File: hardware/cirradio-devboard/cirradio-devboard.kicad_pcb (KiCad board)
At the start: 10 copper layers, 0 parts

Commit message: configure 10-layer stackup and design rules
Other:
- board outline added: 160 x 100 mm
- net class DDR3 added: clearance 0.1, trace_width 0.1, via_dia 0.45, via_drill 0.2
- net class DDR3_DiffPair added: clearance 0.1, trace_width 0.1, via_dia 0.45, via_drill 0.2
- net class Default added: clearance 0.1, trace_width 0.15, via_dia 0.55, via_drill 0.3
- net class LVDS added: clearance 0.12, trace_width 0.12, via_dia 0.45, via_drill 0.2
- net class Power added: clearance 0.2, trace_width 0.4, via_dia 0.7, via_drill 0.4
- net class Power_Wide added: clearance 0.2, trace_width 0.8, via_dia 0.7, via_drill 0.4
- net class RF_50ohm added: clearance 0.2, trace_width 0.28, via_dia 0.55, via_drill 0.3
- board text added: "IMPEDANCE TARGETS: 50u03A9 microstrip (F.Cu): 0.28mm w, ref GND1 100u03A9 diff stripline (In2.Cu): 0.12mm w, 0.20mm gap 50u03A9 stripline (In2/In4.Cu): 0.18mm w"
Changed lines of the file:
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@@
     (pad_to_mask_clearance 0)
     (allow_soldermask_bridges_in_footprints no)
+    (stackup
+      (layer "F.Cu" (type "copper") (thickness 0.035))
+      (layer "dielectric 1" (type "prepreg") (thickness 0.1) (epsilon_r 4.2))
+      (layer "In1.Cu" (type "copper") (thickness 0.035))
+      (layer "dielectric 2" (type "core") (thickness 0.2) (epsilon_r 4.5))
+      (layer "In2.Cu" (type "copper") (thickness 0.035))
+      (layer "dielectric 3" (type "prepreg") (thickness 0.1) (epsilon_r 4.2))
+      (layer "In3.Cu" (type "copper") (thickness 0.035))
+      (layer "dielectric 4" (type "core") (thickness 0.2) (epsilon_r 4.5))
+      (layer "In4.Cu" (type "copper") (thickness 0.035))
+      (layer "dielectric 5" (type "prepreg") (thickness 0.1) (epsilon_r 4.2))
+      (layer "In5.Cu" (type "copper") (thickness 0.035))
+      (layer "dielectric 6" (type "core") (thickness 0.2) (epsilon_r 4.5))
+      (layer "In6.Cu" (type "copper") (thickness 0.035))
+      (layer "dielectric 7" (type "prepreg") (thickness 0.1) (epsilon_r 4.2))
+      (layer "In7.Cu" (type "copper") (thickness 0.035))
+      (layer "dielectric 8" (type "core") (thickness 0.2) (epsilon_r 4.5))
+      (layer "In8.Cu" (type "copper") (thickness 0.035))
+      (layer "dielectric 9" (type "prepreg") (thickness 0.1) (epsilon_r 4.2))
+      (layer "B.Cu" (type "copper") (thickness 0.035))
+      (copper_finish "ENIG")
+      (dielectric_constraints yes)
+    )
     (pcbplotparams
       (layerselection 0x00010fc_ffffffff)
@@
   (net 0 "")
   (net 1 "GND")
+  (net_class "Default" ""
+    (clearance 0.1)
+    (trace_width 0.15)
+    (via_dia 0.55)
+    (via_drill 0.3)
+    (uvia_dia 0.3)
+    (uvia_drill 0.1)
+  )
+  (net_class "Power" ""
+    (clearance 0.2)
+    (trace_width 0.4)
+    (via_dia 0.7)
+    (via_drill 0.4)
+    (uvia_dia 0.3)
+    (uvia_drill 0.1)
+  )
+  (net_class "Power_Wide" ""
+    (clearance 0.2)
+    (trace_width 0.8)
+    (via_dia 0.7)
+    (via_drill 0.4)
+    (uvia_dia 0.3)
+    (uvia_drill 0.1)
+  )
+  (net_class "RF_50ohm" ""
+    (clearance 0.2)
+    (trace_width 0.28)
+    (via_dia 0.55)
+    (via_drill 0.3)
+    (uvia_dia 0.3)
+    (uvia_drill 0.1)
+  )
+  (net_class "LVDS" ""
+    (clearance 0.12)
+    (trace_width 0.12)
+    (via_dia 0.45)
+    (via_drill 0.2)
+    (uvia_dia 0.3)
+    (uvia_drill 0.1)
+    (diff_pair_width 0.12)
+    (diff_pair_gap 0.2)
+  )
+  (net_class "DDR3" ""
+    (clearance 0.1)
+    (trace_width 0.1)
+    (via_dia 0.45)
+    (via_drill 0.2)
+    (uvia_dia 0.3)
+    (uvia_drill 0.1)
+  )
+  (net_class "DDR3_DiffPair" ""
+    (clearance 0.1)
+    (trace_width 0.1)
+    (via_dia 0.45)
+    (via_drill 0.2)
+    (uvia_dia 0.3)
+    (uvia_drill 0.1)
+    (diff_pair_width 0.1)
+    (diff_pair_gap 0.15)
+  )
+  (gr_rect (start 0 0) (end 160 100) (stroke (width 0.1) (type solid)) (fill none) (layer "Edge.Cuts"))
+  (gr_text "IMPEDANCE TARGETS:\n50\u03A9 microstrip (F.Cu): 0.28mm w, ref GND1\n100\u03A9 diff stripline (In2.Cu): 0.12mm w, 0.20mm gap\n50\u03A9 stripline (In2/In4.Cu): 0.18mm w"
+    (at 80 -5) (layer "Cmts.User")
+    (effects (font (size 1.5 1.5) (thickness 0.15)))
+  )
 )

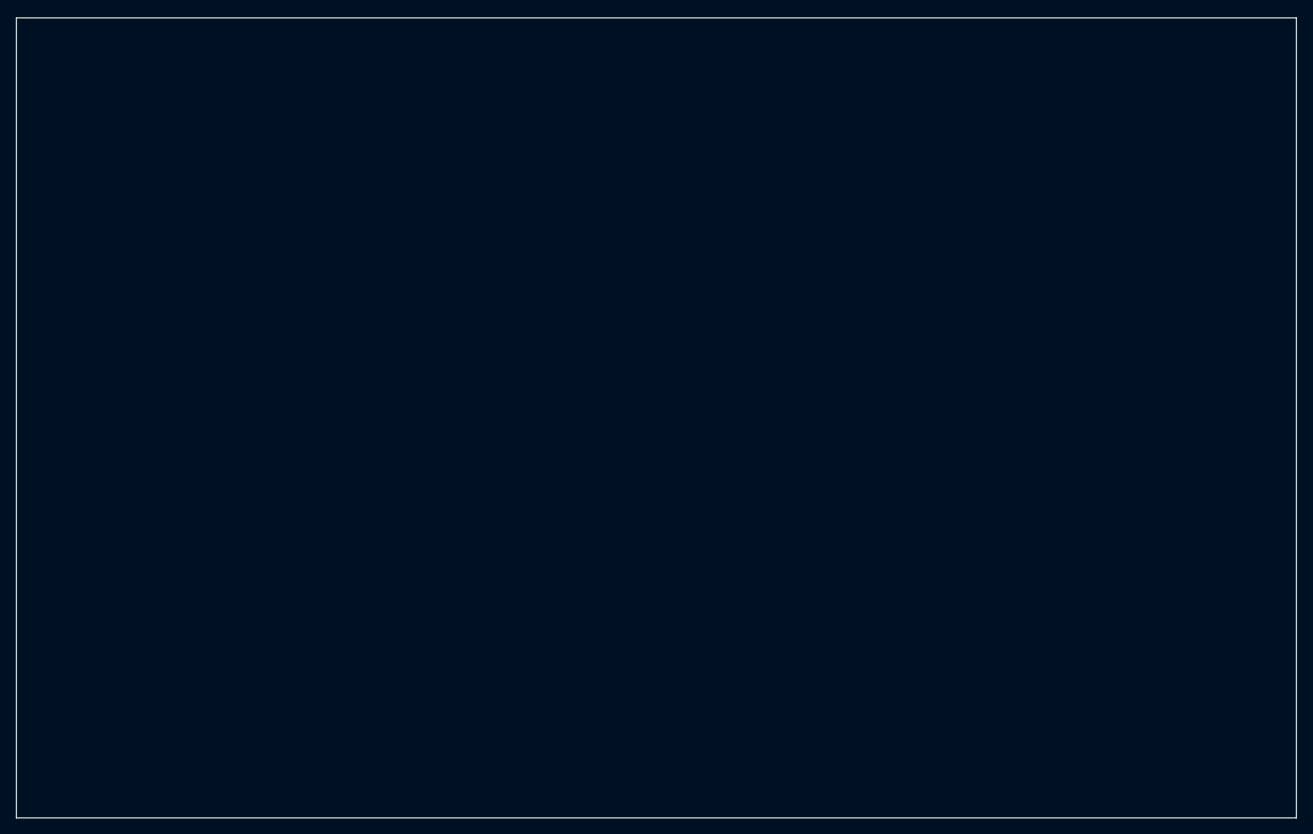
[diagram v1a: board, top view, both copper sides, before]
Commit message: add PCB netlist import with board setup
312 components, 433 nets parsed from schematics.
10-layer stackup, net classes (DDR3, LVDS, RF, Power),
160x100mm board outline, 4x M3 mounting holes.
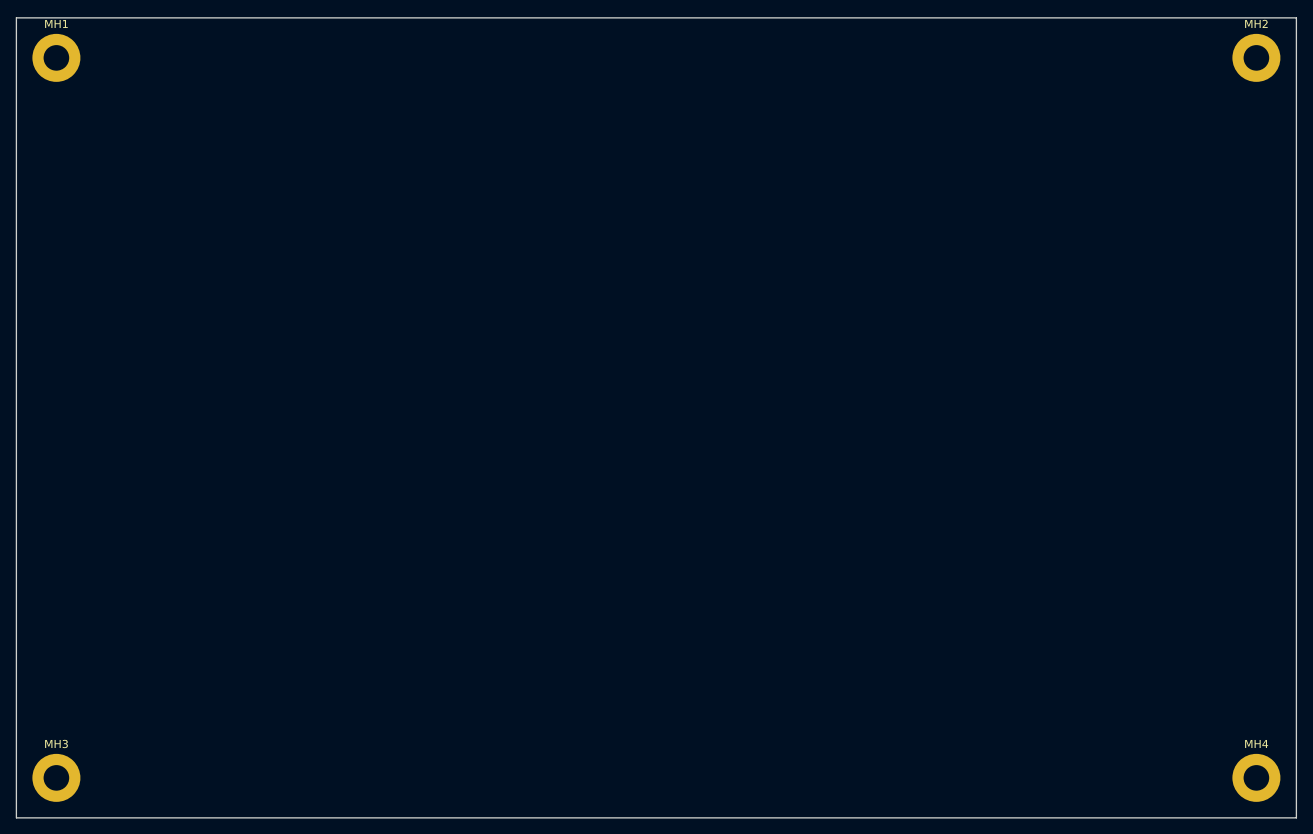
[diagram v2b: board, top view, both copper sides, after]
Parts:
- added MH1: MountingHole_3.2mm_M3_Pad, MountingHole:MountingHole_3.2mm_M3_Pad, F.Cu at (5.00, 5.00)
- added MH2: MountingHole_3.2mm_M3_Pad, MountingHole:MountingHole_3.2mm_M3_Pad, F.Cu at (155.0, 5.00)
- added MH3: MountingHole_3.2mm_M3_Pad, MountingHole:MountingHole_3.2mm_M3_Pad, F.Cu at (5.00, 95.0)
- added MH4: MountingHole_3.2mm_M3_Pad, MountingHole:MountingHole_3.2mm_M3_Pad, F.Cu at (155.0, 95.0)
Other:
- board text added: "NETLIST IMPORT SUMMARY: Total components: 312 Total nets: 433 ICs: 16, Caps: 181, Res: 72, Ind: 13, Diodes: 4, LEDs: 4 Connectors: 7, Crystals: 3 Note: Run Update PCB from Schematic to import component footprints"

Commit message: add component placement generator
312 components placed across 7 zones: RF front-end,
AD9361, Zynq center, DDR3L, power supply, GPS,
connectors. Decoupling caps on B.Cu under BGAs.
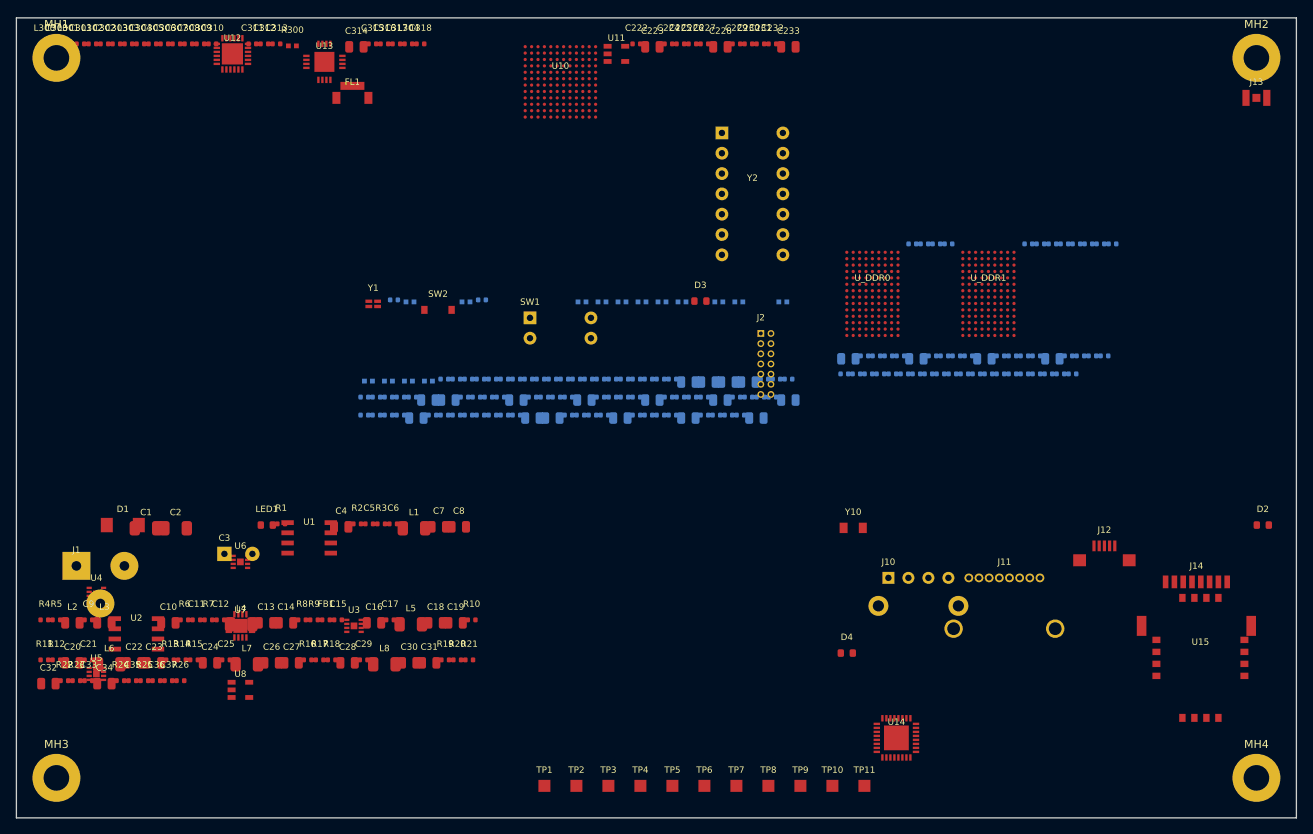
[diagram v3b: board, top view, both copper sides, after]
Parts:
- added C1: 100uF, Capacitor_SMD:C_1206_3216Metric, F.Cu at (16.2, 63.8)
- added C10: 10uF, Capacitor_SMD:C_0805_2012Metric, F.Cu at (19.0, 75.6)
- added C100: 100n, Capacitor_SMD:C_0402_1005Metric, B.Cu at (47.2, 35.2)
- added C101: 100n, Capacitor_SMD:C_0402_1005Metric, B.Cu at (58.2, 35.2)
- added C102: 100n, Capacitor_SMD:C_0402_1005Metric, B.Cu at (53.5, 45.1)
- added C103: 100n, Capacitor_SMD:C_0402_1005Metric, B.Cu at (55.0, 45.1)
- added C104: 100n, Capacitor_SMD:C_0402_1005Metric, B.Cu at (56.5, 45.1)
- added C105: 100n, Capacitor_SMD:C_0402_1005Metric, B.Cu at (58.0, 45.1)
- added C106: 100n, Capacitor_SMD:C_0402_1005Metric, B.Cu at (59.5, 45.1)
- added C107: 100n, Capacitor_SMD:C_0402_1005Metric, B.Cu at (61.0, 45.1)
- added C108: 100n, Capacitor_SMD:C_0402_1005Metric, B.Cu at (62.5, 45.1)
- added C109: 100n, Capacitor_SMD:C_0402_1005Metric, B.Cu at (64.0, 45.1)
- added C11: 100nF, Capacitor_SMD:C_0402_1005Metric, F.Cu at (22.5, 75.2)
- added C110: 100n, Capacitor_SMD:C_0402_1005Metric, B.Cu at (65.5, 45.1)
- added C111: 100n, Capacitor_SMD:C_0402_1005Metric, B.Cu at (67.0, 45.1)
- added C112: 100n, Capacitor_SMD:C_0402_1005Metric, B.Cu at (68.5, 45.1)
- added C113: 100n, Capacitor_SMD:C_0402_1005Metric, B.Cu at (70.0, 45.1)
- added C114: 100n, Capacitor_SMD:C_0402_1005Metric, B.Cu at (71.5, 45.1)
- added C115: 100n, Capacitor_SMD:C_0402_1005Metric, B.Cu at (73.0, 45.1)
- added C116: 100n, Capacitor_SMD:C_0402_1005Metric, B.Cu at (74.5, 45.1)
- added C117: 100n, Capacitor_SMD:C_0402_1005Metric, B.Cu at (76.0, 45.1)
- added C118: 100n, Capacitor_SMD:C_0402_1005Metric, B.Cu at (77.5, 45.1)
- added C119: 100n, Capacitor_SMD:C_0402_1005Metric, B.Cu at (79.0, 45.1)
- added C12: 2.2nF, Capacitor_SMD:C_0402_1005Metric, F.Cu at (25.5, 75.2)
- added C120: 100n, Capacitor_SMD:C_0402_1005Metric, B.Cu at (80.5, 45.1)
- added C121: 100n, Capacitor_SMD:C_0402_1005Metric, B.Cu at (82.0, 45.1)
- added C122: 10u, Capacitor_SMD:C_0805_2012Metric, B.Cu at (84.0, 45.5)
- added C123: 10u, Capacitor_SMD:C_0805_2012Metric, B.Cu at (86.5, 45.5)
- added C124: 10u, Capacitor_SMD:C_0805_2012Metric, B.Cu at (89.0, 45.5)
- added C125: 10u, Capacitor_SMD:C_0805_2012Metric, B.Cu at (91.5, 45.5)
- added C126: 100n, Capacitor_SMD:C_0402_1005Metric, B.Cu at (93.5, 45.1)
- added C127: 100n, Capacitor_SMD:C_0402_1005Metric, B.Cu at (95.0, 45.1)
- added C128: 100n, Capacitor_SMD:C_0402_1005Metric, B.Cu at (96.5, 45.1)
- added C129: 100n, Capacitor_SMD:C_0402_1005Metric, B.Cu at (43.5, 47.4)
- added C13: 22uF, Capacitor_SMD:C_0805_2012Metric, F.Cu at (31.2, 75.6)
- added C130: 100n, Capacitor_SMD:C_0402_1005Metric, B.Cu at (45.0, 47.4)
- added C131: 100n, Capacitor_SMD:C_0402_1005Metric, B.Cu at (46.5, 47.4)
- added C132: 100n, Capacitor_SMD:C_0402_1005Metric, B.Cu at (48.0, 47.4)
- added C133: 100n, Capacitor_SMD:C_0402_1005Metric, B.Cu at (49.5, 47.4)
- added C134: 10u, Capacitor_SMD:C_0805_2012Metric, B.Cu at (51.5, 47.8)
- added C135: 10u, Capacitor_SMD:C_0805_2012Metric, B.Cu at (54.0, 47.8)
- added C136: 100n, Capacitor_SMD:C_0402_1005Metric, B.Cu at (56.0, 47.4)
- added C137: 100n, Capacitor_SMD:C_0402_1005Metric, B.Cu at (57.5, 47.4)
- added C138: 100n, Capacitor_SMD:C_0402_1005Metric, B.Cu at (59.0, 47.4)
- added C139: 100n, Capacitor_SMD:C_0402_1005Metric, B.Cu at (60.5, 47.4)
- added C14: 22uF, Capacitor_SMD:C_0805_2012Metric, F.Cu at (33.7, 75.6)
- added C140: 10u, Capacitor_SMD:C_0805_2012Metric, B.Cu at (62.5, 47.8)
- added C141: 100n, Capacitor_SMD:C_0402_1005Metric, B.Cu at (64.5, 47.4)
- added C142: 100n, Capacitor_SMD:C_0402_1005Metric, B.Cu at (66.0, 47.4)
- added C143: 100n, Capacitor_SMD:C_0402_1005Metric, B.Cu at (67.5, 47.4)
- added C144: 100n, Capacitor_SMD:C_0402_1005Metric, B.Cu at (69.0, 47.4)
- added C145: 10u, Capacitor_SMD:C_0805_2012Metric, B.Cu at (71.0, 47.8)
- added C146: 100n, Capacitor_SMD:C_0402_1005Metric, B.Cu at (73.0, 47.4)
- added C147: 100n, Capacitor_SMD:C_0402_1005Metric, B.Cu at (74.5, 47.4)
- added C148: 100n, Capacitor_SMD:C_0402_1005Metric, B.Cu at (76.0, 47.4)
- added C149: 100n, Capacitor_SMD:C_0402_1005Metric, B.Cu at (77.5, 47.4)
- added C15: 100nF, Capacitor_SMD:C_0402_1005Metric, F.Cu at (40.2, 75.2)
- added C150: 10u, Capacitor_SMD:C_0805_2012Metric, B.Cu at (79.5, 47.8)
- added C151: 100n, Capacitor_SMD:C_0402_1005Metric, B.Cu at (81.5, 47.4)
- added C152: 100n, Capacitor_SMD:C_0402_1005Metric, B.Cu at (83.0, 47.4)
- added C153: 100n, Capacitor_SMD:C_0402_1005Metric, B.Cu at (84.5, 47.4)
- added C154: 100n, Capacitor_SMD:C_0402_1005Metric, B.Cu at (86.0, 47.4)
- added C155: 10u, Capacitor_SMD:C_0805_2012Metric, B.Cu at (88.0, 47.8)
- added C156: 100n, Capacitor_SMD:C_0402_1005Metric, B.Cu at (90.0, 47.4)
- added C157: 100n, Capacitor_SMD:C_0402_1005Metric, B.Cu at (91.5, 47.4)
- added C158: 100n, Capacitor_SMD:C_0402_1005Metric, B.Cu at (93.0, 47.4)
- added C159: 100n, Capacitor_SMD:C_0402_1005Metric, B.Cu at (94.5, 47.4)
- added C16: 10uF, Capacitor_SMD:C_0805_2012Metric, F.Cu at (44.7, 75.6)
- added C160: 10u, Capacitor_SMD:C_0805_2012Metric, B.Cu at (96.5, 47.8)
- added C161: 100n, Capacitor_SMD:C_0402_1005Metric, B.Cu at (43.5, 49.6)
- added C162: 100n, Capacitor_SMD:C_0402_1005Metric, B.Cu at (45.0, 49.6)
- added C163: 100n, Capacitor_SMD:C_0402_1005Metric, B.Cu at (46.5, 49.6)
- added C164: 100n, Capacitor_SMD:C_0402_1005Metric, B.Cu at (48.0, 49.6)
- added C165: 10u, Capacitor_SMD:C_0805_2012Metric, B.Cu at (50.0, 50.0)
- added C166: 100n, Capacitor_SMD:C_0402_1005Metric, B.Cu at (52.0, 49.6)
- added C167: 100n, Capacitor_SMD:C_0402_1005Metric, B.Cu at (53.5, 49.6)
- added C168: 100n, Capacitor_SMD:C_0402_1005Metric, B.Cu at (55.0, 49.6)
- added C169: 100n, Capacitor_SMD:C_0402_1005Metric, B.Cu at (56.5, 49.6)
- added C17: 10nF, Capacitor_SMD:C_0402_1005Metric, F.Cu at (46.7, 75.2)
- added C170: 100n, Capacitor_SMD:C_0402_1005Metric, B.Cu at (58.0, 49.6)
- added C171: 100n, Capacitor_SMD:C_0402_1005Metric, B.Cu at (59.5, 49.6)
- added C172: 100n, Capacitor_SMD:C_0402_1005Metric, B.Cu at (61.0, 49.6)
- added C173: 100n, Capacitor_SMD:C_0402_1005Metric, B.Cu at (62.5, 49.6)
- added C174: 10u, Capacitor_SMD:C_0805_2012Metric, B.Cu at (64.5, 50.0)
- added C175: 10u, Capacitor_SMD:C_0805_2012Metric, B.Cu at (67.0, 50.0)
- added C176: 100n, Capacitor_SMD:C_0402_1005Metric, B.Cu at (69.0, 49.6)
- added C177: 100n, Capacitor_SMD:C_0402_1005Metric, B.Cu at (70.5, 49.6)
- added C178: 100n, Capacitor_SMD:C_0402_1005Metric, B.Cu at (72.0, 49.6)
- added C179: 100n, Capacitor_SMD:C_0402_1005Metric, B.Cu at (73.5, 49.6)
- added C18: 22uF, Capacitor_SMD:C_0805_2012Metric, F.Cu at (52.4, 75.6)
- added C180: 10u, Capacitor_SMD:C_0805_2012Metric, B.Cu at (75.5, 50.0)
- added C181: 100n, Capacitor_SMD:C_0402_1005Metric, B.Cu at (77.5, 49.6)
- added C182: 100n, Capacitor_SMD:C_0402_1005Metric, B.Cu at (79.0, 49.6)
- added C183: 100n, Capacitor_SMD:C_0402_1005Metric, B.Cu at (80.5, 49.6)
- added C184: 100n, Capacitor_SMD:C_0402_1005Metric, B.Cu at (82.0, 49.6)
- added C185: 10u, Capacitor_SMD:C_0805_2012Metric, B.Cu at (84.0, 50.0)
- added C186: 100n, Capacitor_SMD:C_0402_1005Metric, B.Cu at (86.0, 49.6)
- added C187: 100n, Capacitor_SMD:C_0402_1005Metric, B.Cu at (87.5, 49.6)
- added C188: 100n, Capacitor_SMD:C_0402_1005Metric, B.Cu at (89.0, 49.6)
- added C189: 100n, Capacitor_SMD:C_0402_1005Metric, B.Cu at (90.5, 49.6)
- added C19: 22uF, Capacitor_SMD:C_0805_2012Metric, F.Cu at (54.9, 75.6)
- added C190: 10u, Capacitor_SMD:C_0805_2012Metric, B.Cu at (92.5, 50.0)
- added C2: 100uF, Capacitor_SMD:C_1206_3216Metric, F.Cu at (19.9, 63.8)
- added C20: 10uF, Capacitor_SMD:C_0805_2012Metric, F.Cu at (7.00, 80.6)
- added C200: 100n, Capacitor_SMD:C_0402_1005Metric, B.Cu at (116.5, 28.2)
- added C201: 100n, Capacitor_SMD:C_0402_1005Metric, B.Cu at (131.0, 28.2)
- added C202: 100n, Capacitor_SMD:C_0402_1005Metric, B.Cu at (132.5, 28.2)
- added C203: 100n, Capacitor_SMD:C_0402_1005Metric, B.Cu at (134.0, 28.2)
- added C204: 100n, Capacitor_SMD:C_0402_1005Metric, B.Cu at (135.5, 28.2)
- added C205: 100n, Capacitor_SMD:C_0402_1005Metric, B.Cu at (137.0, 28.2)
- added C206: 10u, Capacitor_SMD:C_0805_2012Metric, B.Cu at (104.0, 42.6)
- added C207: 100n, Capacitor_SMD:C_0402_1005Metric, B.Cu at (106.0, 42.2)
- added C208: 100n, Capacitor_SMD:C_0402_1005Metric, B.Cu at (107.5, 42.2)
- added C209: 100n, Capacitor_SMD:C_0402_1005Metric, B.Cu at (109.0, 42.2)
- added C21: 10nF, Capacitor_SMD:C_0402_1005Metric, F.Cu at (9.00, 80.2)
- added C210: 100n, Capacitor_SMD:C_0402_1005Metric, B.Cu at (110.5, 42.2)
- added C211: 10u, Capacitor_SMD:C_0805_2012Metric, B.Cu at (112.5, 42.6)
- added C212: 100n, Capacitor_SMD:C_0402_1005Metric, B.Cu at (114.5, 42.2)
- added C213: 100n, Capacitor_SMD:C_0402_1005Metric, B.Cu at (116.0, 42.2)
- added C214: 100n, Capacitor_SMD:C_0402_1005Metric, B.Cu at (117.5, 42.2)
- added C215: 100n, Capacitor_SMD:C_0402_1005Metric, B.Cu at (119.0, 42.2)
- added C216: 10u, Capacitor_SMD:C_0805_2012Metric, B.Cu at (121.0, 42.6)
- added C217: 100n, Capacitor_SMD:C_0402_1005Metric, B.Cu at (123.0, 42.2)
- added C218: 100n, Capacitor_SMD:C_0402_1005Metric, B.Cu at (124.5, 42.2)
- added C219: 100n, Capacitor_SMD:C_0402_1005Metric, B.Cu at (126.0, 42.2)
- added C22: 22uF, Capacitor_SMD:C_0805_2012Metric, F.Cu at (14.7, 80.6)
- added C220: 100n, Capacitor_SMD:C_0402_1005Metric, B.Cu at (127.5, 42.2)
- added C221: 10u, Capacitor_SMD:C_0805_2012Metric, B.Cu at (129.5, 42.6)
- added C222: 100n, Capacitor_SMD:C_0402_1005Metric, F.Cu at (77.5, 3.25)
- added C223: 10u, Capacitor_SMD:C_0805_2012Metric, F.Cu at (79.5, 3.62)
- added C224: 100n, Capacitor_SMD:C_0402_1005Metric, F.Cu at (81.5, 3.25)
- added C225: 100n, Capacitor_SMD:C_0402_1005Metric, F.Cu at (83.0, 3.25)
- added C226: 100n, Capacitor_SMD:C_0402_1005Metric, F.Cu at (84.5, 3.25)
- added C227: 100n, Capacitor_SMD:C_0402_1005Metric, F.Cu at (86.0, 3.25)
- added C228: 10u, Capacitor_SMD:C_0805_2012Metric, F.Cu at (88.0, 3.62)
- added C229: 100n, Capacitor_SMD:C_0402_1005Metric, F.Cu at (90.0, 3.25)
- added C23: 22uF, Capacitor_SMD:C_0805_2012Metric, F.Cu at (17.2, 80.6)
- added C230: 100n, Capacitor_SMD:C_0402_1005Metric, F.Cu at (91.5, 3.25)
- added C231: 100n, Capacitor_SMD:C_0402_1005Metric, F.Cu at (93.0, 3.25)
- added C232: 100n, Capacitor_SMD:C_0402_1005Metric, F.Cu at (94.5, 3.25)
- added C233: 10u, Capacitor_SMD:C_0805_2012Metric, F.Cu at (96.5, 3.62)
- added C24: 10uF, Capacitor_SMD:C_0805_2012Metric, F.Cu at (24.2, 80.6)
- added C25: 10nF, Capacitor_SMD:C_0402_1005Metric, F.Cu at (26.2, 80.2)
- added C26: 22uF, Capacitor_SMD:C_0805_2012Metric, F.Cu at (31.9, 80.6)
- added C27: 22uF, Capacitor_SMD:C_0805_2012Metric, F.Cu at (34.4, 80.6)
- added C28: 10uF, Capacitor_SMD:C_0805_2012Metric, F.Cu at (41.4, 80.6)
- added C29: 10nF, Capacitor_SMD:C_0402_1005Metric, F.Cu at (43.4, 80.2)
- added C3: 470uF, Capacitor_THT:CP_Radial_D8.0mm_P3.50mm, F.Cu at (26.0, 67.0)
- added C30: 22uF, Capacitor_SMD:C_0805_2012Metric, F.Cu at (49.1, 80.6)
- added C300: 22p, Capacitor_SMD:C_0402_1005Metric, F.Cu at (5.00, 3.25)
- added C301: 22p, Capacitor_SMD:C_0402_1005Metric, F.Cu at (8.00, 3.25)
- added C302: 22p, Capacitor_SMD:C_0402_1005Metric, F.Cu at (11.0, 3.25)
- added C303: 100n, Capacitor_SMD:C_0402_1005Metric, F.Cu at (12.5, 3.25)
- added C304: 100n, Capacitor_SMD:C_0402_1005Metric, F.Cu at (15.5, 3.25)
- added C305: 10n, Capacitor_SMD:C_0402_1005Metric, F.Cu at (17.0, 3.25)
- added C306: 100n, Capacitor_SMD:C_0402_1005Metric, F.Cu at (18.5, 3.25)
- added C307: 100p, Capacitor_SMD:C_0402_1005Metric, F.Cu at (20.0, 3.25)
- added C308: 100p, Capacitor_SMD:C_0402_1005Metric, F.Cu at (21.5, 3.25)
- added C309: 100p, Capacitor_SMD:C_0402_1005Metric, F.Cu at (23.0, 3.25)
- added C31: 22uF, Capacitor_SMD:C_0805_2012Metric, F.Cu at (51.6, 80.6)
- added C310: 100p, Capacitor_SMD:C_0402_1005Metric, F.Cu at (24.5, 3.25)
- added C311: 100n, Capacitor_SMD:C_0402_1005Metric, F.Cu at (29.5, 3.25)
- added C312: 10n, Capacitor_SMD:C_0402_1005Metric, F.Cu at (31.0, 3.25)
- added C313: 100n, Capacitor_SMD:C_0402_1005Metric, F.Cu at (32.5, 3.25)
- added C314: 10u, Capacitor_SMD:C_0805_2012Metric, F.Cu at (42.5, 3.62)
- added C315: 100n, Capacitor_SMD:C_0402_1005Metric, F.Cu at (44.5, 3.25)
- added C316: 10n, Capacitor_SMD:C_0402_1005Metric, F.Cu at (46.0, 3.25)
- added C317: 33p, Capacitor_SMD:C_0402_1005Metric, F.Cu at (47.5, 3.25)
- added C318: 33p, Capacitor_SMD:C_0402_1005Metric, F.Cu at (50.5, 3.25)
- added C32: 10uF, Capacitor_SMD:C_0805_2012Metric, F.Cu at (4.00, 83.2)
- added C33: 100nF, Capacitor_SMD:C_0402_1005Metric, F.Cu at (9.00, 82.8)
- added C34: 47uF, Capacitor_SMD:C_0805_2012Metric, F.Cu at (11.0, 83.2)
- added C35: 100nF, Capacitor_SMD:C_0402_1005Metric, F.Cu at (14.5, 82.8)
- added C36: 100nF, Capacitor_SMD:C_0402_1005Metric, F.Cu at (17.5, 82.8)
- added C37: 100nF, Capacitor_SMD:C_0402_1005Metric, F.Cu at (19.0, 82.8)
- added C4: 10uF, Capacitor_SMD:C_0805_2012Metric, F.Cu at (40.6, 63.6)
- added C5: 100nF, Capacitor_SMD:C_0402_1005Metric, F.Cu at (44.1, 63.2)
- added C6: 2.2nF, Capacitor_SMD:C_0402_1005Metric, F.Cu at (47.1, 63.2)
- added C7: 22uF, Capacitor_SMD:C_0805_2012Metric, F.Cu at (52.8, 63.6)
- added C8: 22uF, Capacitor_SMD:C_0805_2012Metric, F.Cu at (55.3, 63.6)
- added C9: 100nF, Capacitor_SMD:C_0402_1005Metric, F.Cu at (9.00, 75.2)
- added D1: SS34, Diode_SMD:D_SMA, F.Cu at (13.3, 63.4)
- added D2: Green, LED_SMD:LED_0603_1608Metric, F.Cu at (155.8, 63.4)
- added D3: GREEN, LED_SMD:LED_0603_1608Metric, F.Cu at (85.5, 35.4)
- added D4: Green, LED_SMD:LED_0603_1608Metric, F.Cu at (103.8, 79.4)
- added FB1: 600R@100MHz, Inductor_SMD:L_0402_1005Metric, F.Cu at (38.7, 75.2)
- added FL1: SAW 225-512MHz, cirradio:FL1, F.Cu at (42.0, 10.0)
- added J1: 12V DC Input, Connector_BarrelJack:BarrelJack_Horizontal, F.Cu at (7.50, 68.5)
- added J10: USB_A, Connector_USB:USB_A_Molex_105057_Vertical, F.Cu at (109.0, 70.0)
- added J11: RJ45_MagJack, Connector_RJ:RJ45_Amphenol_ARJM11D7, F.Cu at (123.5, 70.0)
- added J12: USB_Micro_B, Connector_USB:USB_Micro-B_Molex_47346-0001, F.Cu at (136.0, 66.0)
- added J13: U.FL_GPS, Connector_Coaxial:U.FL_Hirose_U.FL-R-SMT-1_Vertical, F.Cu at (155.0, 10.0)
- added J14: Micro_SD, Connector_Card:microSD_HC_Hirose_DM3D-SF, F.Cu at (147.5, 70.5)
- added J2: JTAG, Connector_PinHeader_1.27mm:PinHeader_2x07_P1.27mm_Vertical, F.Cu at (93.0, 39.5)
- added L1: 10uH, Inductor_SMD:L_1210_3225Metric, F.Cu at (49.7, 63.8)
- added L2: 100nH, Inductor_SMD:L_0805_2012Metric, F.Cu at (7.00, 75.6)
- added L3: 100nH, Inductor_SMD:L_0805_2012Metric, F.Cu at (11.0, 75.6)
- added L300: 47n, Inductor_SMD:L_0402_1005Metric, F.Cu at (3.50, 3.25)
- added L301: 47n, Inductor_SMD:L_0402_1005Metric, F.Cu at (6.50, 3.25)
- added L302: 47n, Inductor_SMD:L_0402_1005Metric, F.Cu at (9.50, 3.25)
- added L303: 100n, Inductor_SMD:L_0402_1005Metric, F.Cu at (14.0, 3.25)
- added L304: 27n, Inductor_SMD:L_0402_1005Metric, F.Cu at (49.0, 3.25)
- added L4: 10uH, Inductor_SMD:L_1210_3225Metric, F.Cu at (28.1, 75.8)
- added L5: 2.2uH, Inductor_SMD:L_1210_3225Metric, F.Cu at (49.3, 75.8)
- added L6: 3.3uH, Inductor_SMD:L_1210_3225Metric, F.Cu at (11.6, 80.8)
- added L7: 3.3uH, Inductor_SMD:L_1210_3225Metric, F.Cu at (28.8, 80.8)
- added L8: 3.3uH, Inductor_SMD:L_1210_3225Metric, F.Cu at (46.0, 80.8)
- added LED1: Green, LED_SMD:LED_0603_1608Metric, F.Cu at (31.3, 63.4)
- added R1: 4.7K, Resistor_SMD:R_0402_1005Metric, F.Cu at (33.1, 63.2)
- added R10: 100K, Resistor_SMD:R_0402_1005Metric, F.Cu at (56.9, 75.2)
- added R100: 22R, cirradio:R100, B.Cu at (49.2, 35.5)
- added R101: 10K, cirradio:R101, B.Cu at (56.2, 35.5)
- added R102: 10K, cirradio:R102, B.Cu at (70.7, 35.5)
- added R103: 10K, cirradio:R103, B.Cu at (73.2, 35.5)
- added R104: 10K, cirradio:R104, B.Cu at (75.7, 35.5)
- added R105: 10K, cirradio:R105, B.Cu at (78.2, 35.5)
- added R106: 4K7, cirradio:R106, B.Cu at (80.7, 35.5)
- added R107: 330R, cirradio:R107, B.Cu at (83.2, 35.5)
- added R108: 4K7, cirradio:R108, B.Cu at (87.8, 35.5)
- added R109: 4K7, cirradio:R109, B.Cu at (90.3, 35.5)
- added R11: 100K, Resistor_SMD:R_0402_1005Metric, F.Cu at (3.50, 80.2)
- added R110: 33R, cirradio:R110, B.Cu at (95.8, 35.5)
- added R111: 33R, cirradio:R111, B.Cu at (44.0, 45.4)
- added R112: 33R, cirradio:R112, B.Cu at (46.5, 45.4)
- added R113: 240R, cirradio:R113, B.Cu at (49.0, 45.4)
- added R114: 240R, cirradio:R114, B.Cu at (51.5, 45.4)
- added R12: 100K, Resistor_SMD:R_0402_1005Metric, F.Cu at (5.00, 80.2)
- added R13: 200K, Resistor_SMD:R_0402_1005Metric, F.Cu at (19.2, 80.2)
- added R14: 100K, Resistor_SMD:R_0402_1005Metric, F.Cu at (20.7, 80.2)
- added R15: 100K, Resistor_SMD:R_0402_1005Metric, F.Cu at (22.2, 80.2)
- added R16: 261K, Resistor_SMD:R_0402_1005Metric, F.Cu at (36.4, 80.2)
- added R17: 100K, Resistor_SMD:R_0402_1005Metric, F.Cu at (37.9, 80.2)
- added R18: 100K, Resistor_SMD:R_0402_1005Metric, F.Cu at (39.4, 80.2)
- added R19: 169K, Resistor_SMD:R_0402_1005Metric, F.Cu at (53.6, 80.2)
- added R2: 100K, Resistor_SMD:R_0402_1005Metric, F.Cu at (42.6, 63.2)
- added R20: 100K, Resistor_SMD:R_0402_1005Metric, F.Cu at (55.1, 80.2)
- added R200: 240R 1%, Resistor_SMD:R_0402_1005Metric, B.Cu at (112.0, 28.2)
- added R201: 240R, Resistor_SMD:R_0402_1005Metric, B.Cu at (113.5, 28.2)
- added R202: 240R, Resistor_SMD:R_0402_1005Metric, B.Cu at (115.0, 28.2)
- added R203: 240R 1%, Resistor_SMD:R_0402_1005Metric, B.Cu at (126.5, 28.2)
- added R204: 240R, Resistor_SMD:R_0402_1005Metric, B.Cu at (128.0, 28.2)
- added R205: 240R, Resistor_SMD:R_0402_1005Metric, B.Cu at (129.5, 28.2)
- added R206: 47R, Resistor_SMD:R_0402_1005Metric, B.Cu at (131.5, 42.2)
- added R207: 47R, Resistor_SMD:R_0402_1005Metric, B.Cu at (133.0, 42.2)
- added R208: 47R, Resistor_SMD:R_0402_1005Metric, B.Cu at (134.5, 42.2)
- added R209: 47R, Resistor_SMD:R_0402_1005Metric, B.Cu at (136.0, 42.2)
- added R21: 100K, Resistor_SMD:R_0402_1005Metric, F.Cu at (56.6, 80.2)
- added R210: 47R, Resistor_SMD:R_0402_1005Metric, B.Cu at (103.5, 44.5)
- added R211: 47R, Resistor_SMD:R_0402_1005Metric, B.Cu at (105.0, 44.5)
- added R212: 47R, Resistor_SMD:R_0402_1005Metric, B.Cu at (106.5, 44.5)
- added R213: 47R, Resistor_SMD:R_0402_1005Metric, B.Cu at (108.0, 44.5)
- added R214: 47R, Resistor_SMD:R_0402_1005Metric, B.Cu at (109.5, 44.5)
- added R215: 47R, Resistor_SMD:R_0402_1005Metric, B.Cu at (111.0, 44.5)
- added R216: 47R, Resistor_SMD:R_0402_1005Metric, B.Cu at (112.5, 44.5)
- added R217: 47R, Resistor_SMD:R_0402_1005Metric, B.Cu at (114.0, 44.5)
- added R218: 47R, Resistor_SMD:R_0402_1005Metric, B.Cu at (115.5, 44.5)
- added R219: 47R, Resistor_SMD:R_0402_1005Metric, B.Cu at (117.0, 44.5)
- added R22: 10K, Resistor_SMD:R_0402_1005Metric, F.Cu at (6.00, 82.8)
- added R220: 47R, Resistor_SMD:R_0402_1005Metric, B.Cu at (118.5, 44.5)
- added R221: 47R, Resistor_SMD:R_0402_1005Metric, B.Cu at (120.0, 44.5)
- added R222: 47R, Resistor_SMD:R_0402_1005Metric, B.Cu at (121.5, 44.5)
- added R223: 47R, Resistor_SMD:R_0402_1005Metric, B.Cu at (123.0, 44.5)
- added R224: 47R, Resistor_SMD:R_0402_1005Metric, B.Cu at (124.5, 44.5)
- added R225: 47R, Resistor_SMD:R_0402_1005Metric, B.Cu at (126.0, 44.5)
- added R226: 47R, Resistor_SMD:R_0402_1005Metric, B.Cu at (127.5, 44.5)
- added R227: 47R, Resistor_SMD:R_0402_1005Metric, B.Cu at (129.0, 44.5)
- added R228: 47R, Resistor_SMD:R_0402_1005Metric, B.Cu at (130.5, 44.5)
- added R229: 47R, Resistor_SMD:R_0402_1005Metric, B.Cu at (132.0, 44.5)
- added R23: 10K, Resistor_SMD:R_0402_1005Metric, F.Cu at (7.50, 82.8)
- added R24: 100K, Resistor_SMD:R_0402_1005Metric, F.Cu at (13.0, 82.8)
- added R25: 100K, Resistor_SMD:R_0402_1005Metric, F.Cu at (16.0, 82.8)
- added R26: 10K, Resistor_SMD:R_0402_1005Metric, F.Cu at (20.5, 82.8)
- added R3: 10K, Resistor_SMD:R_0402_1005Metric, F.Cu at (45.6, 63.2)
- added R300: 49.9, cirradio:R300, F.Cu at (34.5, 3.50)
- added R4: 52.3K, Resistor_SMD:R_0402_1005Metric, F.Cu at (3.50, 75.2)
- added R5: 10K, Resistor_SMD:R_0402_1005Metric, F.Cu at (5.00, 75.2)
- added R6: 100K, Resistor_SMD:R_0402_1005Metric, F.Cu at (21.0, 75.2)
- added R7: 10K, Resistor_SMD:R_0402_1005Metric, F.Cu at (24.0, 75.2)
- added R8: 31.6K, Resistor_SMD:R_0402_1005Metric, F.Cu at (35.7, 75.2)
- added R9: 10K, Resistor_SMD:R_0402_1005Metric, F.Cu at (37.2, 75.2)
- added SW1: BOOT_MODE, Button_Switch_SMD:SW_DIP_SPSTx02_Slide_6.7x6.64mm_W8.61mm_P2.54mm, F.Cu at (64.2, 37.5)
- added SW2: RESET, Button_Switch_SMD:SW_SPST_B3U-1000P, F.Cu at (52.7, 36.5)
- added TP1: +12V, TestPoint:TestPoint_Pad_1.5x1.5mm, F.Cu at (66.0, 96.0)
- added TP10: GPS_1PPS, TestPoint:TestPoint_Pad_1.5x1.5mm, F.Cu at (102.0, 96.0)
- added TP11: PS_CLK, TestPoint:TestPoint_Pad_1.5x1.5mm, F.Cu at (106.0, 96.0)
- added TP2: +5V, TestPoint:TestPoint_Pad_1.5x1.5mm, F.Cu at (70.0, 96.0)
- added TP3: +3V3, TestPoint:TestPoint_Pad_1.5x1.5mm, F.Cu at (74.0, 96.0)
- added TP4: +1V8, TestPoint:TestPoint_Pad_1.5x1.5mm, F.Cu at (78.0, 96.0)
- added TP5: +1V35, TestPoint:TestPoint_Pad_1.5x1.5mm, F.Cu at (82.0, 96.0)
- added TP6: +1V0, TestPoint:TestPoint_Pad_1.5x1.5mm, F.Cu at (86.0, 96.0)
- added TP7: +1V5, TestPoint:TestPoint_Pad_1.5x1.5mm, F.Cu at (90.0, 96.0)
- added TP8: VTT, TestPoint:TestPoint_Pad_1.5x1.5mm, F.Cu at (94.0, 96.0)
- added TP9: GND, TestPoint:TestPoint_Pad_1.5x1.5mm, F.Cu at (98.0, 96.0)
- added U1: TPS54360B (5.0V), cirradio:SOIC-8_3.9x4.9mm_P1.27mm, F.Cu at (36.6, 65.0)
- added U10: AD9361BBCZ, cirradio:BGA-144_12x12_0.8mm, F.Cu at (68.0, 8.00)
- added U11: ADP151-1.3, cirradio:SOT-23-5, F.Cu at (75.0, 4.50)
- added U12: ADL5606ACPZ, Package_DFN_QFN:QFN-24-1EP_4x4mm_P0.5mm_EP2.65x2.65mm, F.Cu at (27.0, 4.50)
- added U13: TGA2594-SM, cirradio:TGA2594-SM, F.Cu at (38.5, 5.50)
- added U14: FT232RQ, Package_DFN_QFN:QFN-32-1EP_5x5mm_P0.5mm_EP3.1x3.1mm, F.Cu at (110.0, 90.0)
- added U15: MAX-M10S, cirradio:LCC-16_MAX-M10S, F.Cu at (148.0, 80.0)
- added U2: TPS54360B (3.3V), cirradio:SOIC-8_3.9x4.9mm_P1.27mm, F.Cu at (15.0, 77.0)
- added U3: TPS62913 (1.0V), cirradio:WSON-8_2x2mm_P0.5mm, F.Cu at (42.2, 76.0)
- added U4: TPS62913 (1.5V), cirradio:WSON-8_2x2mm_P0.5mm, F.Cu at (10.0, 72.0)
- added U5: TPS62913 (1.8V), cirradio:WSON-8_2x2mm_P0.5mm, F.Cu at (10.0, 82.0)
- added U6: TPS62913 (1.35V), cirradio:WSON-8_2x2mm_P0.5mm, F.Cu at (28.0, 68.0)
- added U7: TPS51200, cirradio:QFN-16_3x3mm_P0.5mm, F.Cu at (28.0, 76.0)
- added U8: TPS3808G01, cirradio:SOT-23-5.kicad_mod, F.Cu at (28.0, 84.0)
- added U_DDR0: MT41K256M16HA-125, cirradio:BGA-96_9x14_0.8mm, F.Cu at (107.0, 34.5)
- added U_DDR1: MT41K256M16HA-125, cirradio:BGA-96_9x14_0.8mm, F.Cu at (121.5, 34.5)
- added Y1: 33.333MHz, Package_SO:VDFN-4-1EP_2.5x2.0mm_P0.65mm, F.Cu at (44.6, 35.8)
- added Y10: 25MHz, Crystal:Crystal_SMD_3215-2Pin_3.2x1.5mm, F.Cu at (104.6, 63.8)
- added Y2: 40.000MHz OCXO, cirradio:DIP-14_W7.62mm, F.Cu at (92.0, 22.0)

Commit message: add power and ground plane generator
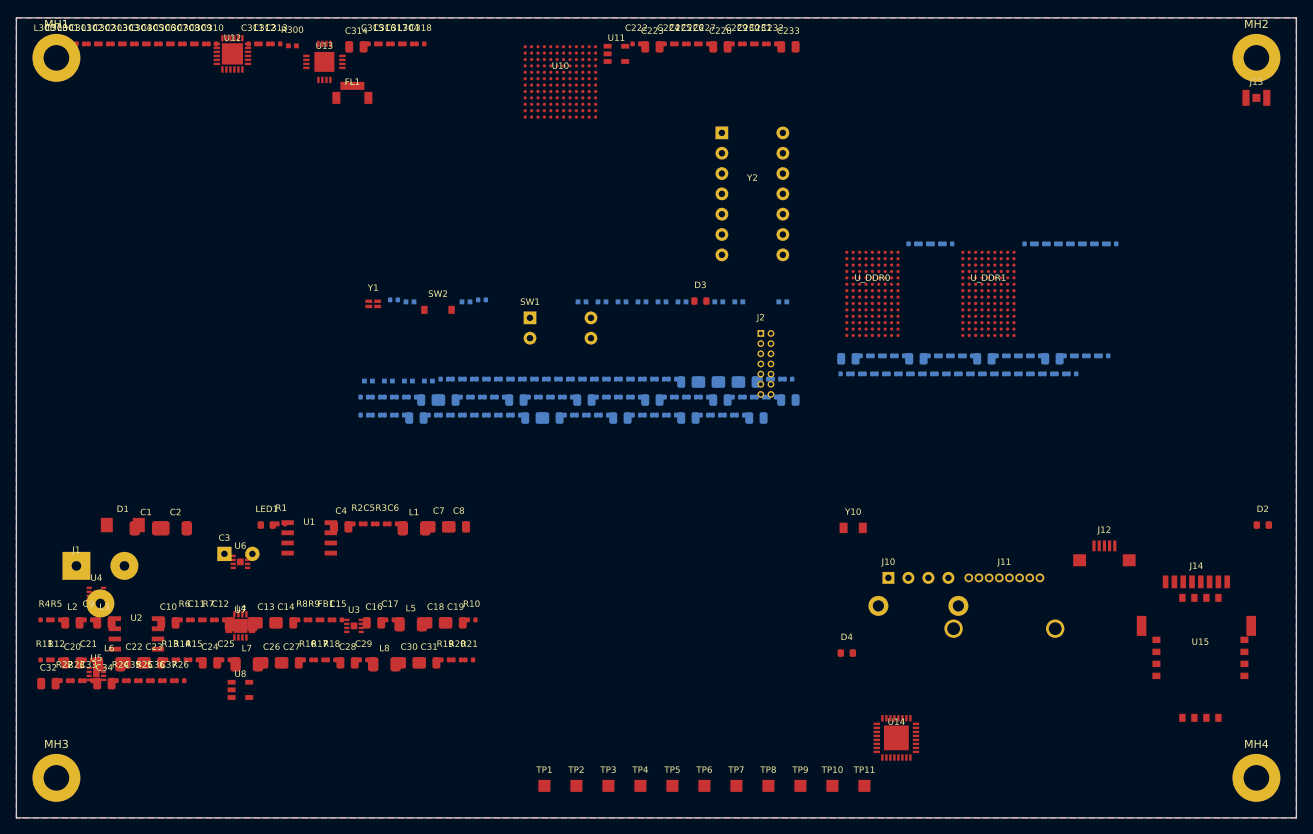
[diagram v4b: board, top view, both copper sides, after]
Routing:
- added copper zone on In5.Cu, net +1V0
- added copper zone on In5.Cu, net +1V35
- added copper zone on In5.Cu, net +1V5
- added copper zone on In5.Cu, net +1V8
- added copper zone on In5.Cu, net +3V3
- added copper zone on In5.Cu, net +5V
- added copper zone on B.Cu, net GND
- added copper zone on F.Cu, net GND
- added copper zone on In1.Cu, net GND
- added copper zone on In3.Cu, net GND
- added copper zone on In7.Cu, net GND

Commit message: add PCB routing and via stitching generator
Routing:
- net +1V3_AD: track 0.00 -> 84.4 mm
- net +3V3A: track 0.00 -> 78.2 mm
- net AD_TX1A: track 0.00 -> 73.6 mm
- net +12V: track 0.00 -> 71.6 mm
- net AD_RX1A_P: track 0.00 -> 70.4 mm
- net MIO10: track 0.00 -> 66.2 mm
- net MIO11: track 0.00 -> 64.3 mm
- net +1V0: track 0.00 -> 62.6 mm
- net MIO12: track 0.00 -> 62.3 mm
- net MIO13: track 0.00 -> 60.3 mm
- net +1V8: track 0.00 -> 58.5 mm
- net PS_UART0_RX: track 0.00 -> 56.8 mm
- net PS_UART0_TX: track 0.00 -> 55.9 mm
- net +5V: track 0.00 -> 55.2 mm
- net +3V3: track 0.00 -> 55.2 mm
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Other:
- board text added: "CIRRADIO DevBoard v1.0"
- board text added: "DDR3L"
- board text added: "FPGA"
- board text added: "POWER"
- board text added: "RF"
- board text added: "Zynq-7045 + AD9361"
